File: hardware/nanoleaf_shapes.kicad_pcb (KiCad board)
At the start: 2 copper layers, 35.6 x 21.5 mm, 42 parts, among them J1 Conn_01x03, J2 Conn_01x03, SW1 RESET, SW2 BOOT, U1 TPS54360DDAR, U2 WT0132C6-S5, U3 74LVC1G125GV_C52140413, U4 74LVC1G125GV_C52140413

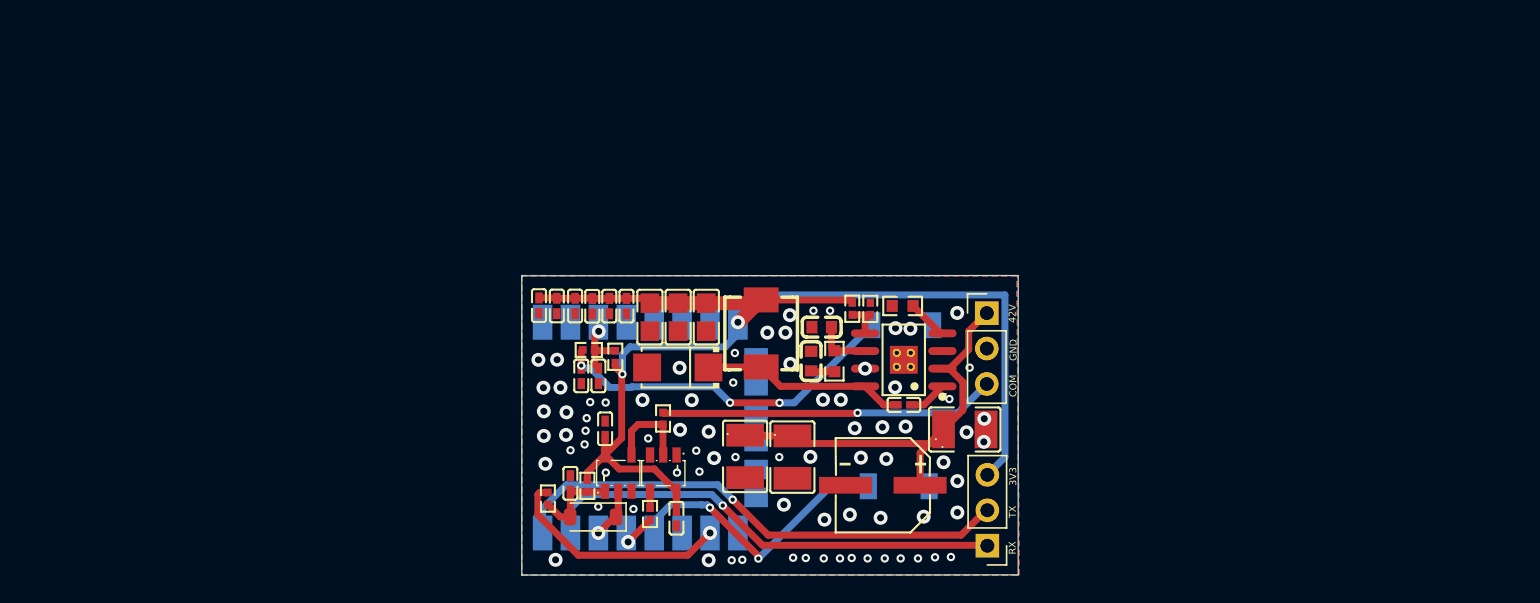
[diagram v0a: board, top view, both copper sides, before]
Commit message: Rev B hardware: replaces rev A, not yet verified
Rev B clips onto a panel like the stock controller instead of connecting
through a cut flex linker, and fixes the rev A issues listed in the README.
It replaces rev A in hardware/.

NOT VERIFIED. No rev B board has been built or powered up. Boards are on
order. What has been checked is DRC (0 errors, 0 unconnected items), ground
continuity, a 3D fit check of the enclosure against the KiCad component
models, and the fabrication files against the board they came from. None of
that proves the circuit works. Rev A, which is built and working, stays in
the history at the previous commit.

Also added:

- mechanical/ builds the enclosure from the board itself. export_parts.py
  dumps the geometry out of KiCad, enclosure.py turns it into a tray, a lid
  and three separate button caps, and make_fab_files.py writes the BOM and
  placement files. case_v1_working/ keeps the previous enclosure as a
  fallback, with the sources and parts.json that produced it.
- fab/pcbway/ holds the gerbers, drill files, BOM and centroid file.
- render/ holds three KiCad 3D renders, shown in the README.

The JLCPCB fabrication files are deliberately not published. PCBWay are
sponsoring this board, and that file set also carries corrections that only
make sense against JLCPCB's own library.

Co-Authored-By: Claude Opus 5 <noreply@anthropic.com>
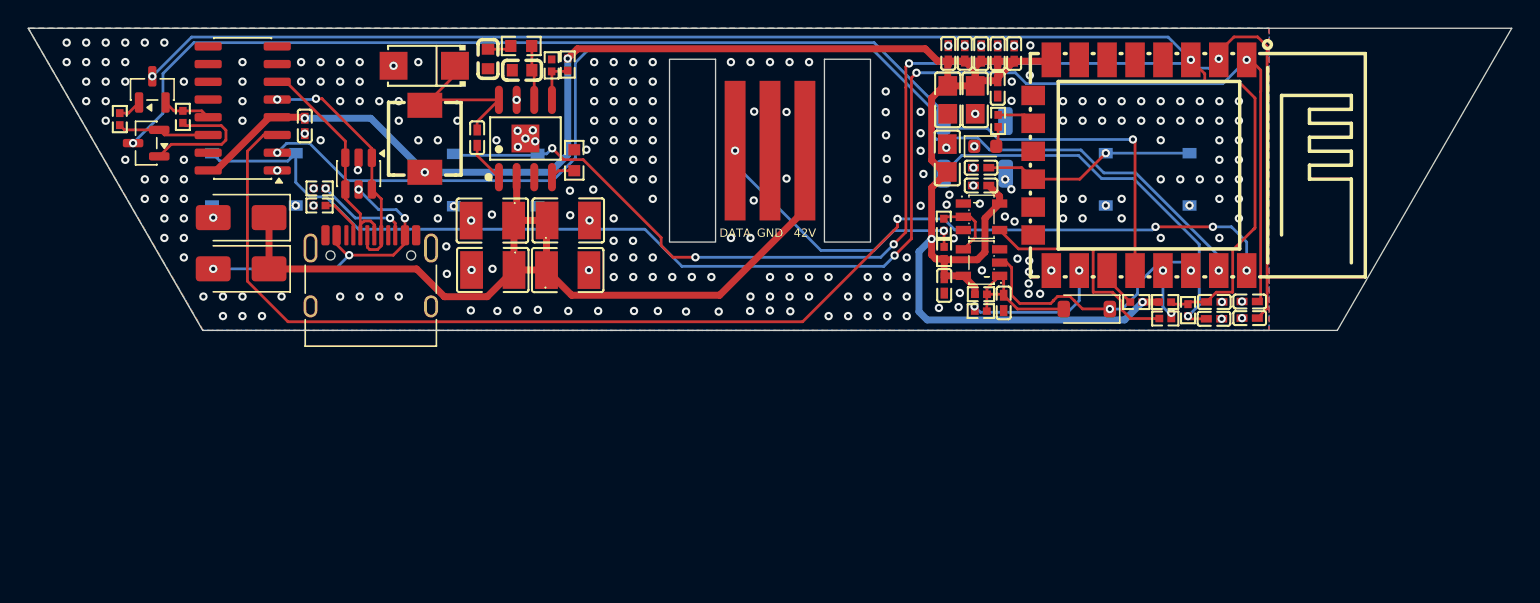
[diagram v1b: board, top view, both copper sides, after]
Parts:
- removed J2: Conn_01x03, Connector_PinHeader_2.54mm:PinHeader_1x03_P2.54mm_Vertical
- added C22: 100nF 16V, easyeda2kicad:C0402, F.Cu at (53.5, 53.0)
- added C23: 100nF 16V, easyeda2kicad:C0402, F.Cu at (121.2, 65.6)
- added C24: 100nF 16V, easyeda2kicad:C0402, F.Cu at (121.2, 66.8)
- added C26: 100nF 16V, easyeda2kicad:C0402, F.Cu at (102.0, 56.0)
- added D3: SMAJ48A, Diode_SMD:D_SMA, F.Cu at (48.9, 59.6)
- added D4: LED, LED_SMD:LED_0603_1608Metric, F.Cu at (102.3, 54.5)
- added D5: 100V/2A Schottky, Diode_SMD:D_SMA, F.Cu at (48.9, 63.2)
- added J3: USB_C_Receptacle_USB2.0_16P, Connector_USB:USB_C_Receptacle_HRO_TYPE-C-31-M-12, F.Cu at (58.2, 64.9)
- added Q1: MMBT3904, Package_TO_SOT_SMD:SOT-23, F.Cu at (42.1, 54.2)
- added Q2: MMBT3904, Package_TO_SOT_SMD:SOT-23, F.Cu at (42.6, 50.4)
- added R11: 5.1k, easyeda2kicad:R0402, F.Cu at (54.6, 58.7)
- added R12: 5.1k, easyeda2kicad:R0402, F.Cu at (54.6, 57.5)
- added R13: 10k, easyeda2kicad:R0402, F.Cu at (44.8, 52.3)
- added R14: 10k, easyeda2kicad:R0402, F.Cu at (40.2, 52.5)
- added R15: 100k, easyeda2kicad:R0402, F.Cu at (99.3, 62.1)
- added R16: 10k, easyeda2kicad:R0402, F.Cu at (113.1, 65.6)
- added R17: 1k, easyeda2kicad:R0402, F.Cu at (103.2, 52.6)
- added SW3: USER BUTTON, Button_Switch_SMD:SW_Push_1P1T_XKB_TS-1187A, B.Cu at (49.9, 56.8)
- added SW4: USER BUTTON, Button_Switch_SMD:SW_Push_1P1T_XKB_TS-1187A, B.Cu at (67.2, 56.9)
- added SW6: USER BUTTON, Button_Switch_SMD:SW_Push_1P1T_XKB_TS-1187A, B.Cu at (113.9, 56.8)
- added U5: CH340C, Package_SO:SOIC-16_3.9x9.9mm_P1.27mm, F.Cu at (49.0, 51.7)
- added U6: USBLC6-2SC6, Package_TO_SOT_SMD:SOT-23-6, F.Cu at (57.4, 56.4)
- C11: value 22uF 100V -> 2.2uF 100V; footprint easyeda2kicad:CAP-SMD_BD6.3-L6.6-W6.6-FD-1 -> easyeda2kicad:C1210
- J1: footprint Connector_PinHeader_2.54mm:PinHeader_1x03_P2.54mm_Vertical -> nanoleaf:Nanoleaf_Linker_Pads
- SW1, SW2: footprint easyeda2kicad:SW-SMD_L3.9-W3.0-P4.45 -> Button_Switch_SMD:SW_SPST_TS-1088-xR020
- U2: value WT0132C6-S5 -> ESPC5-12; moved to F.Cu
- moved C20 45.5 mm to (118.7, 66.8), turned to 0 degrees
- moved C21 44.4 mm to (118.7, 65.6), turned to 0 degrees
- moved R8 43.0 mm to (116.8, 66.2), turned to 90 degrees
- moved U2 39.9 mm to (113.3, 55.8), turned to 180 degrees
- moved R9 39.6 mm to (115.2, 65.6), turned to 180 degrees
- moved R6 39.5 mm to (115.2, 66.8), turned to 0 degrees
- moved D2 38.4 mm to (109.5, 66.1)
- moved C4 36.5 mm to (102.0, 47.8), turned to 90 degrees
- moved C5 36.4 mm to (103.2, 47.8), turned to 90 degrees
- moved C6 36.3 mm to (104.3, 47.8), turned to 90 degrees
- moved C10 36.1 mm to (65.8, 53.8), turned to -90 degrees
- moved C1 35.7 mm to (67.0, 63.3), turned to 180 degrees
- moved R10 33.8 mm to (101.9, 66.3), turned to 0 degrees
- moved C17 33.6 mm to (103.6, 65.7), turned to -90 degrees
- moved C18 32.3 mm to (102.0, 57.3), turned to 180 degrees
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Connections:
- net Net-(U2-EN) renamed EN
- net Net-(U2-GPIO9) renamed BOOT
- U2 pad 1: unconnected-(U2-GPIO0-Pad1) -> BTN_PWR
- U2 pad 11: unconnected-(U2-GPIO8-Pad11) -> PAD11
- U2 pad 18: unconnected-(U2-GPIO19-Pad18) -> LED
- U2 pad 2: unconnected-(U2-GPIO1-Pad2) -> BTN_UP
- U2 pad 20: unconnected-(U2-GPIO21-Pad20) -> BTN_DN
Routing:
- net BTN_PWR: track 0.00 -> 110.8 mm, vias 0 -> 3
- net EN: track 4.47 -> 101.7 mm, vias 1 -> 2
- net BTN_UP: track 0.00 -> 96.3 mm, vias 0 -> 5
- net BOOT: track 20.5 -> 89.0 mm
- net TX0: track 36.6 -> 91.1 mm, vias 1 -> 4
- net RX0: track 33.5 -> 85.0 mm, vias 1 -> 2
- net 3V3: track 89.1 -> 136.2 mm, vias 2 -> 5
- net 42V: track 31.8 -> 64.0 mm
- net USB_VBUS: track 0.00 -> 22.4 mm, vias 0 -> 4
- net USB_DP: track 0.00 -> 17.7 mm, vias 0 -> 2
- net USB_DN: track 0.00 -> 16.6 mm
- net BTN_DN: track 0.00 -> 15.5 mm, vias 0 -> 1
- net TX: track 3.66 -> 18.7 mm, vias 1 -> 2
- net Net-(U3-Y): track 1.20 -> 16.2 mm
- net DTR_B: track 0.00 -> 9.27 mm
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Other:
- board size 35.6 x 21.5 mm -> 106.3 x 21.7 mm
- board text removed: "3V3"
- board text removed: "42V"
- board text removed: "COM"
- board text removed: "GND"
- board text removed: "RX"
- board text removed: "TX"
